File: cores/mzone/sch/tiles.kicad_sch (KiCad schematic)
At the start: 37 parts

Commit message: mzone core
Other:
- note removed: "16"
- note removed: "32"
- note removed: "4"
- note removed: "Check SCRY0"
- note removed: "Kolla anslutningar på PCB"
- note removed: "kolla upp FIX anslutningar"
- moved on the sheet: A10, A11, A12, A13, A8, A9, B10A, B10B, B10C, B10D, B11B, B14B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

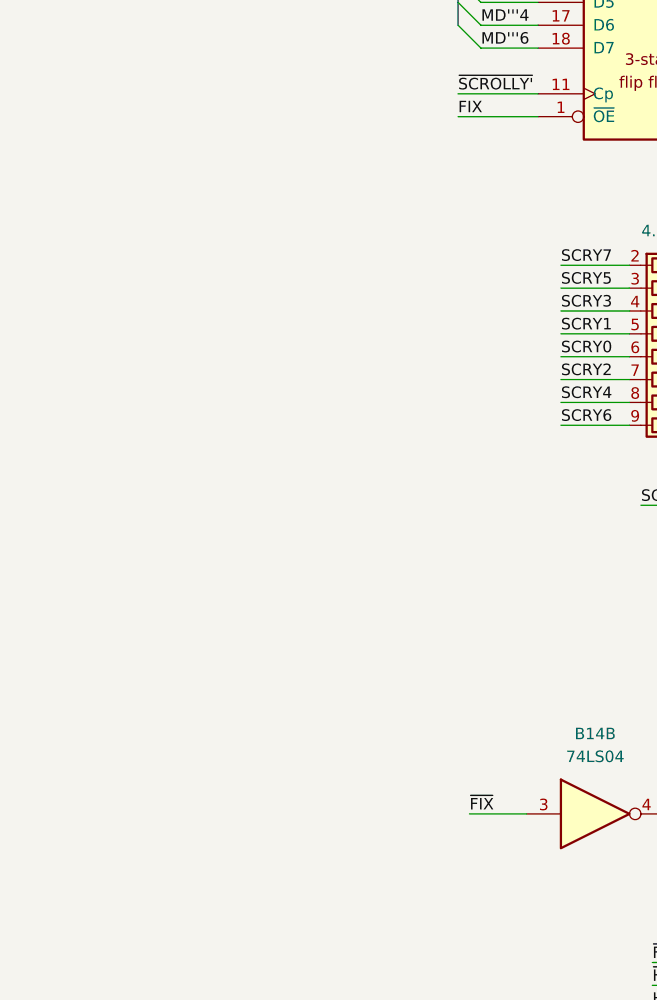
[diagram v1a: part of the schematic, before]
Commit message: mzone core
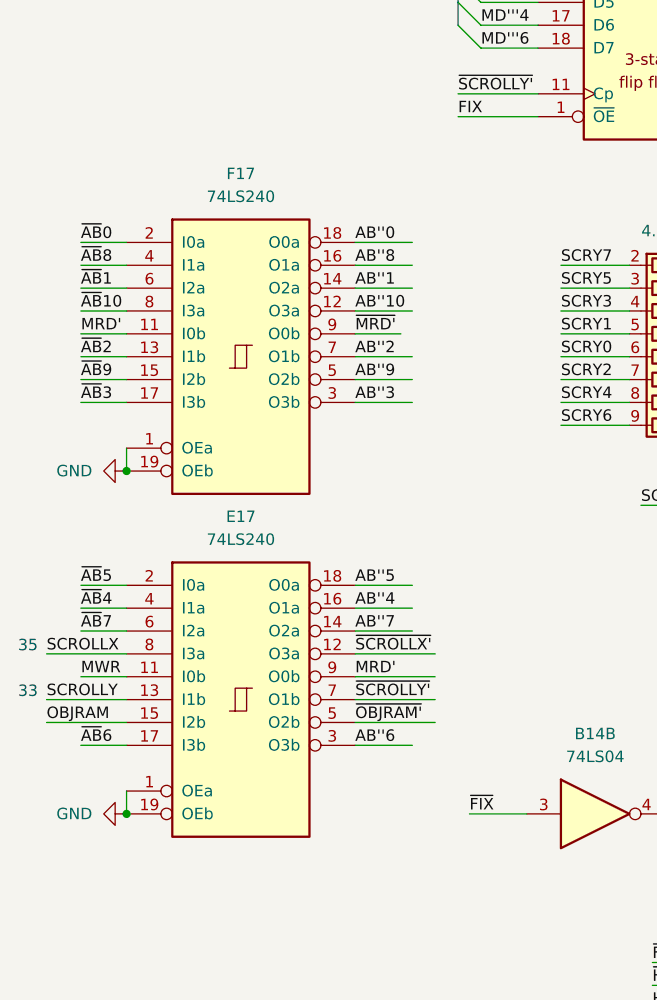
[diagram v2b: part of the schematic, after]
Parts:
- added E17, F17: 74LS240, symbol jt74:74LS240
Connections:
- net AB''0: now also F17.18 (O0a)
- net AB''1: now also F17.14 (O2a)
- net AB''10: now also F17.12 (O3a)
- net AB''2: now also F17.7 (O1b)
- net AB''3: now also F17.3 (O3b)
- net AB''4: now also E17.16 (O1a)
- net AB''5: now also E17.18 (O0a)
- net AB''6: now also E17.3 (O3b)
- net AB''7: now also E17.14 (O2a)
- net AB''8: now also F17.16 (O1a)
- net AB''9: now also F17.5 (O2b)
- net GND: now also E17.1 (OEa), E17.19 (OEb), F17.1 (OEa), F17.19 (OEb)
- net VCC: now also E17.20 (VCC), F17.20 (VCC)
- net VSS: now also E17.10 (VSS), F17.10 (VSS)
- net ~{MRD'}: now also F17.9 (O0b)
- net ~{SCROLLX'}: now also E17.12 (O3a)
- net ~{SCROLLY'}: now also E17.7 (O1b)
- new net MRD': E17.9 (O0b), F17.11 (I0b)
- new net MWR: E17.11 (I0b)
- new net OBJRAM: E17.15 (I2b)
- new net SCROLLX: E17.8 (I3a)
- new net SCROLLY: E17.13 (I1b)
- new net ~{AB}0: F17.2 (I0a)
- new net ~{AB}1: F17.6 (I2a)
- new net ~{AB}10: F17.8 (I3a)
- new net ~{AB}2: F17.13 (I1b)
- new net ~{AB}3: F17.17 (I3b)
- new net ~{AB}4: E17.4 (I1a)
- new net ~{AB}5: E17.2 (I0a)
- new net ~{AB}6: E17.17 (I3b)
- new net ~{AB}7: E17.6 (I2a)
- new net ~{AB}8: F17.4 (I1a)
- new net ~{AB}9: F17.15 (I2b)
- new net ~{OBJRAM'}: E17.5 (O2b)
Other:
- note added: "33"
- note added: "35"

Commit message: mzone core
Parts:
- added C17: 74LS240, symbol 74xx:74LS240_Split
- added unit 2 of D16
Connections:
- net FLIP': now also D16.10, D16.12, D16.13, D16.9
- net ~{COLRAM'}: no longer names the net of D17.12
- net ~{COLRAM'}: now also C17.14
- net ~{FLIP'}: no longer names the net of CD18.5
- net ~{FLIP'}: now also D16.8
- net ~{VRAM'}: no longer names the net of D17.1
- net ~{VRAM'}: now also C17.16
- new net COLRAM: C17.6
- new net VRAM: C17.4
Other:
- note added: "~{FLIP'}"
- note removed: "Delay: HCOUNT 0 to color mixer: G10: HCNT = 1 D8: HCNT = 2 A8: HCNT = 3 A12,A13: HCNT = 4 & PXLCLK pos edge."
- moved on the sheet: A10, A11, A12, A13, A8, A9, B10A, B10B, B10C, B10D, B11B, B14B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

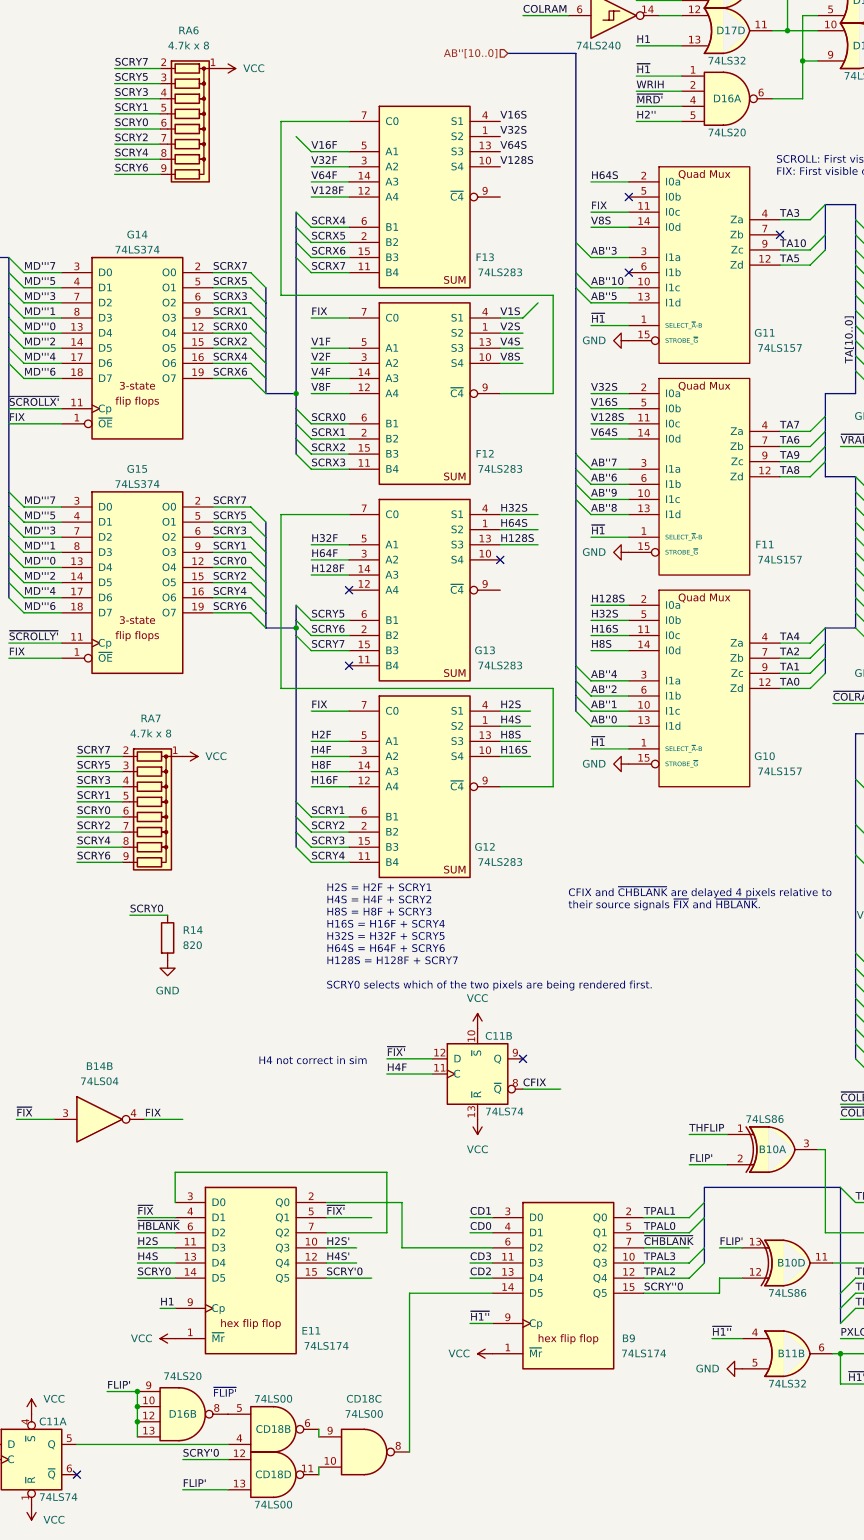
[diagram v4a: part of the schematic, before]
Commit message: mzone core
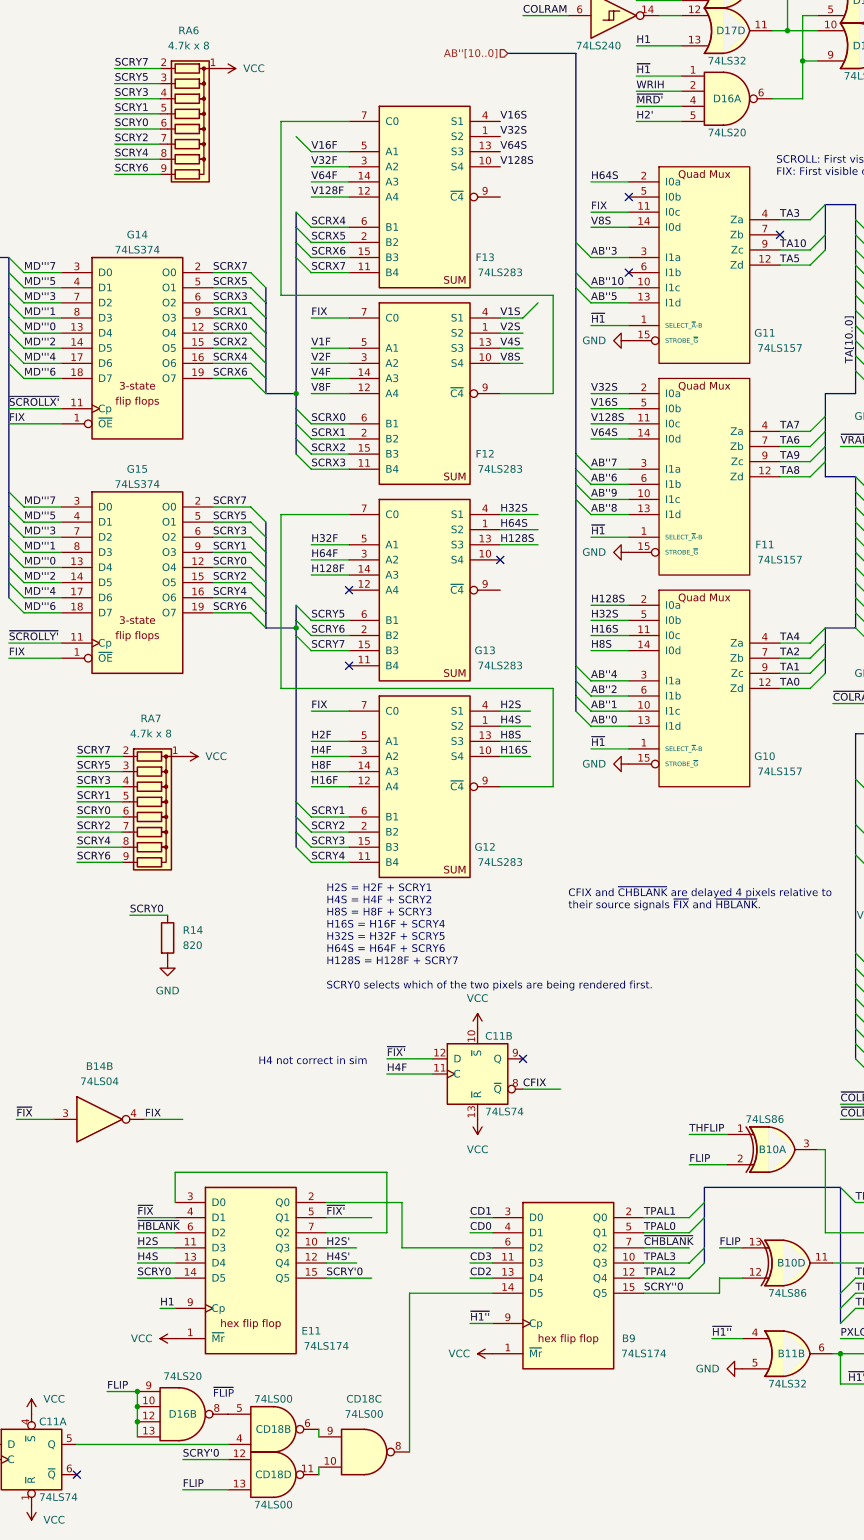
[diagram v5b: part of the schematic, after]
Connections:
- net FLIP' renamed FLIP
- net H2'' renamed H2'
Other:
- note added: "~{FLIP}"
- note removed: "~{FLIP'}"
